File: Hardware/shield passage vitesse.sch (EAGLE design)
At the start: 37 parts, among them Q1 2N7000, Q2 2N7000, Q3 2N7000, Q4 2N7000, Q5 2N7000

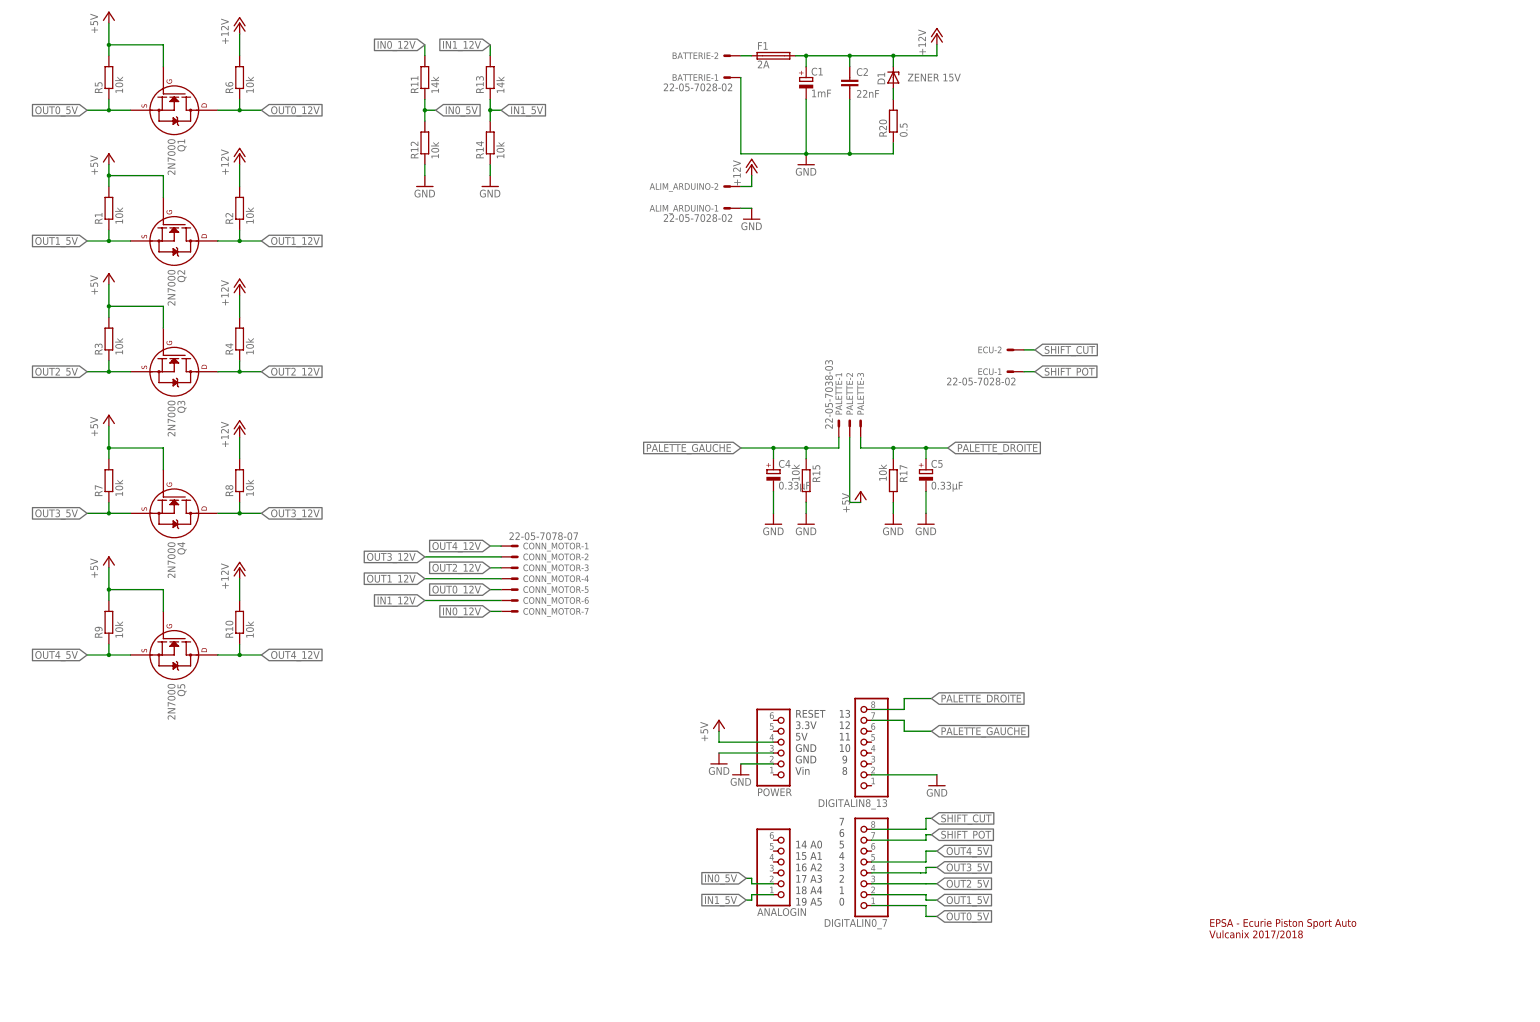
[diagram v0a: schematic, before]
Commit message: Passage de la Zener à 14V
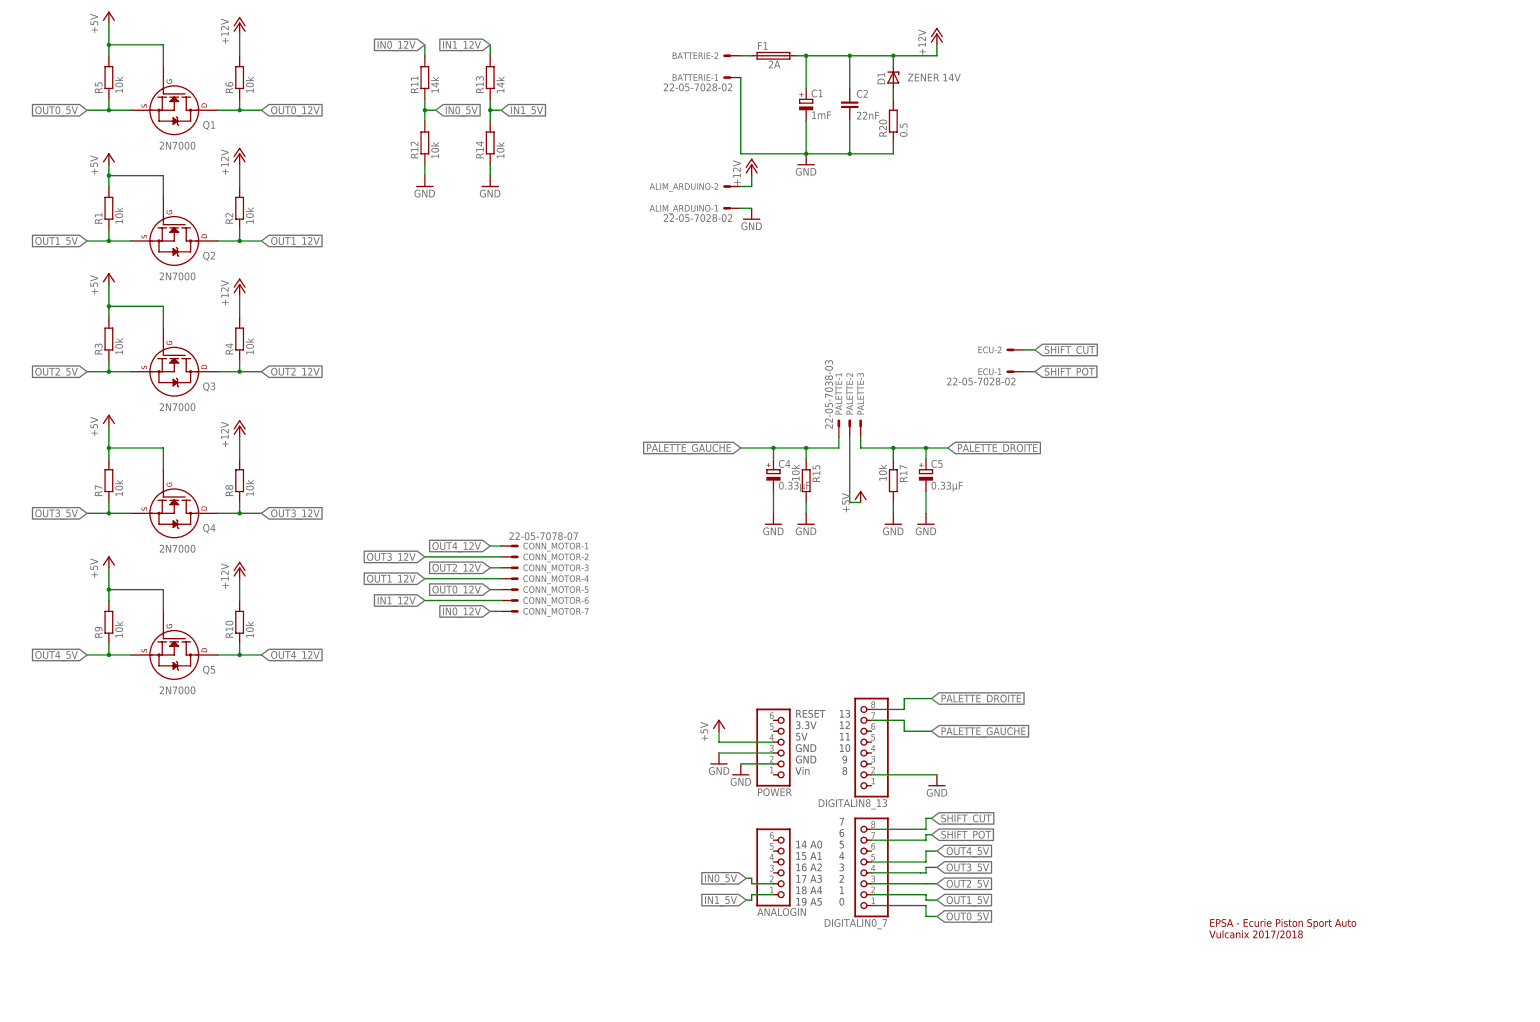
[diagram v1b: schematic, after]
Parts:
- D1: value ZENER 15V -> ZENER 14V
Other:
- moved on the sheet: C1, C2
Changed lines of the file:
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@@
 <part name="FRAME1" library="microbuilder" deviceset="FRAME_A3" device=""/>
 <part name="C2" library="rcl" deviceset="C-EU" device="025-025X050" value="22nF"/>
-<part name="D1" library="diode" deviceset="ZENER-DIODE" device="DO41Z10" value="ZENER 15V"/>
+<part name="D1" library="diode" deviceset="ZENER-DIODE" device="DO41Z10" value="ZENER 14V"/>
 <part name="R20" library="resistor" deviceset="R-EU_" device="0309/12" value="0.5"/>
 <part name="R15" library="resistor" deviceset="R-EU_" device="0204/7" value="10k"/>
@@
 </instance>
 <instance part="Q2" gate="G$1" x="-243.84" y="167.64" smashed="yes" rot="R270">
-<attribute name="NAME" x="-243.078" y="161.036" size="1.778" layer="95" rot="R270"/>
-<attribute name="VALUE" x="-245.364" y="161.036" size="1.778" layer="96" rot="R270"/>
+<attribute name="NAME" x="-237.236" y="163.322" size="1.778" layer="95"/>
+<attribute name="VALUE" x="-247.396" y="158.496" size="1.778" layer="96"/>
 </instance>
 <instance part="R1" gate="G$1" x="-259.08" y="175.26" smashed="yes" rot="R90">
@@
 </instance>
 <instance part="Q3" gate="G$1" x="-243.84" y="137.16" smashed="yes" rot="R270">
-<attribute name="NAME" x="-243.078" y="130.556" size="1.778" layer="95" rot="R270"/>
-<attribute name="VALUE" x="-245.364" y="130.556" size="1.778" layer="96" rot="R270"/>
+<attribute name="NAME" x="-237.236" y="132.842" size="1.778" layer="95"/>
+<attribute name="VALUE" x="-247.396" y="128.016" size="1.778" layer="96"/>
 </instance>
 <instance part="R3" gate="G$1" x="-259.08" y="144.78" smashed="yes" rot="R90">
@@
 </instance>
 <instance part="Q1" gate="G$1" x="-243.84" y="198.12" smashed="yes" rot="R270">
-<attribute name="NAME" x="-243.078" y="191.516" size="1.778" layer="95" rot="R270"/>
-<attribute name="VALUE" x="-245.364" y="191.516" size="1.778" layer="96" rot="R270"/>
+<attribute name="NAME" x="-237.236" y="193.802" size="1.778" layer="95"/>
+<attribute name="VALUE" x="-247.396" y="188.976" size="1.778" layer="96"/>
 </instance>
 <instance part="R5" gate="G$1" x="-259.08" y="205.74" smashed="yes" rot="R90">
@@
 </instance>
 <instance part="Q4" gate="G$1" x="-243.84" y="104.14" smashed="yes" rot="R270">
-<attribute name="NAME" x="-243.078" y="97.536" size="1.778" layer="95" rot="R270"/>
-<attribute name="VALUE" x="-245.364" y="97.536" size="1.778" layer="96" rot="R270"/>
+<attribute name="NAME" x="-237.236" y="99.822" size="1.778" layer="95"/>
+<attribute name="VALUE" x="-247.396" y="94.996" size="1.778" layer="96"/>
 </instance>
 <instance part="R7" gate="G$1" x="-259.08" y="111.76" smashed="yes" rot="R90">
@@
 </instance>
 <instance part="Q5" gate="G$1" x="-243.84" y="71.12" smashed="yes" rot="R270">
-<attribute name="NAME" x="-243.078" y="64.516" size="1.778" layer="95" rot="R270"/>
-<attribute name="VALUE" x="-245.364" y="64.516" size="1.778" layer="96" rot="R270"/>
+<attribute name="NAME" x="-237.236" y="66.802" size="1.778" layer="95"/>
+<attribute name="VALUE" x="-247.396" y="61.976" size="1.778" layer="96"/>
 </instance>
 <instance part="R9" gate="G$1" x="-259.08" y="78.74" smashed="yes" rot="R90">
@@
 <attribute name="VALUE" x="-225.298" y="74.93" size="1.778" layer="96" rot="R90"/>
 </instance>
-<instance part="C1" gate="G$1" x="-96.52" y="205.74" smashed="yes">
-<attribute name="NAME" x="-95.377" y="206.2226" size="1.778" layer="95"/>
-<attribute name="VALUE" x="-95.377" y="201.1426" size="1.778" layer="96"/>
+<instance part="C1" gate="G$1" x="-96.52" y="200.66" smashed="yes">
+<attribute name="NAME" x="-95.377" y="201.1426" size="1.778" layer="95"/>
+<attribute name="VALUE" x="-95.377" y="196.0626" size="1.778" layer="96"/>
 </instance>
 <instance part="GND1" gate="1" x="-96.52" y="185.42" smashed="yes">
@@
 <instance part="F1" gate="1" x="-104.14" y="210.82" smashed="yes">
 <attribute name="NAME" x="-107.95" y="212.217" size="1.778" layer="95"/>
-<attribute name="VALUE" x="-107.95" y="207.899" size="1.778" layer="96"/>
+<attribute name="VALUE" x="-105.41" y="207.899" size="1.778" layer="96"/>
 </instance>
 <instance part="GND3" gate="1" x="-109.22" y="172.72" smashed="yes">
@@
 <attribute name="SHEET" x="55.245" y="-10.16" size="2.54" layer="94" font="vector"/>
 </instance>
-<instance part="C2" gate="G$1" x="-86.36" y="205.74" smashed="yes">
-<attribute name="NAME" x="-84.836" y="206.121" size="1.778" layer="95"/>
-<attribute name="VALUE" x="-84.836" y="201.041" size="1.778" layer="96"/>
+<instance part="C2" gate="G$1" x="-86.36" y="200.66" smashed="yes">
+<attribute name="NAME" x="-84.836" y="201.041" size="1.778" layer="95"/>
+<attribute name="VALUE" x="-84.836" y="195.961" size="1.778" layer="96"/>
 </instance>
 <instance part="D1" gate="G$1" x="-76.2" y="205.74" smashed="yes" rot="R90">
@@
 <wire x1="-111.76" y1="187.96" x2="-96.52" y2="187.96" width="0.1524" layer="91"/>
 <pinref part="C1" gate="G$1" pin="-"/>
-<wire x1="-96.52" y1="187.96" x2="-96.52" y2="200.66" width="0.1524" layer="91"/>
+<wire x1="-96.52" y1="187.96" x2="-96.52" y2="195.58" width="0.1524" layer="91"/>
 <pinref part="GND1" gate="1" pin="GND"/>
 <junction x="-96.52" y="187.96"/>
 <pinref part="C2" gate="G$1" pin="2"/>
 <wire x1="-86.36" y1="187.96" x2="-96.52" y2="187.96" width="0.1524" layer="91"/>
-<wire x1="-86.36" y1="200.66" x2="-86.36" y2="187.96" width="0.1524" layer="91"/>
+<wire x1="-86.36" y1="195.58" x2="-86.36" y2="187.96" width="0.1524" layer="91"/>
 <wire x1="-86.36" y1="187.96" x2="-76.2" y2="187.96" width="0.1524" layer="91"/>
 <wire x1="-76.2" y1="187.96" x2="-76.2" y2="190.5" width="0.1524" layer="91"/>
@@
 <wire x1="-86.36" y1="210.82" x2="-76.2" y2="210.82" width="0.1524" layer="91"/>
 <wire x1="-76.2" y1="210.82" x2="-66.04" y2="210.82" width="0.1524" layer="91"/>
-<wire x1="-96.52" y1="208.28" x2="-96.52" y2="210.82" width="0.1524" layer="91"/>
+<wire x1="-96.52" y1="203.2" x2="-96.52" y2="210.82" width="0.1524" layer="91"/>
 <pinref part="F1" gate="1" pin="2"/>
 <wire x1="-99.06" y1="210.82" x2="-96.52" y2="210.82" width="0.1524" layer="91"/>
 <junction x="-96.52" y="210.82"/>
 <pinref part="C2" gate="G$1" pin="1"/>
-<wire x1="-86.36" y1="208.28" x2="-86.36" y2="210.82" width="0.1524" layer="91"/>
+<wire x1="-86.36" y1="203.2" x2="-86.36" y2="210.82" width="0.1524" layer="91"/>
 <junction x="-86.36" y="210.82"/>
 <pinref part="D1" gate="G$1" pin="C"/>

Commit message: Mise en qualité
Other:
- note added: "Bob AUBOUIN (BAT)"
- note added: "EPSA 2019"
- note added: "Gearbox Controller v1.0"
- note added: "OPTIMUS v1.0"
- note removed: "EPSA - Ecurie Piston Sport Auto Vulcanix 2017/2018"
- moved on the sheet: ALIM_ARDUINO-1, ALIM_ARDUINO-2, ANALOGIN, BATTERIE-1, BATTERIE-2, C1, C2, C4, C5, CONN_MOTOR-1, CONN_MOTOR-2, CONN_MOTOR-3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

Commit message: Passage à la version de dev suivante
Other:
- note added: "Gearbox Controller v2.0-dev"
- note removed: "Gearbox Controller v1.0"
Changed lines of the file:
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@@
 Vin</text>
 <text x="-15.24" y="-10.16" size="3.81" layer="94">Gearbox Controller
-v1.0</text>
+v2.0-dev</text>
 <text x="33.02" y="0" size="2.54" layer="94">EPSA 2019</text>
 <text x="33.02" y="-5.08" size="2.54" layer="94">OPTIMUS v1.0</text>
